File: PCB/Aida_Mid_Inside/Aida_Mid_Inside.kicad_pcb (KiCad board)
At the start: 2 copper layers, 50.3 x 61.6 mm, 24 parts

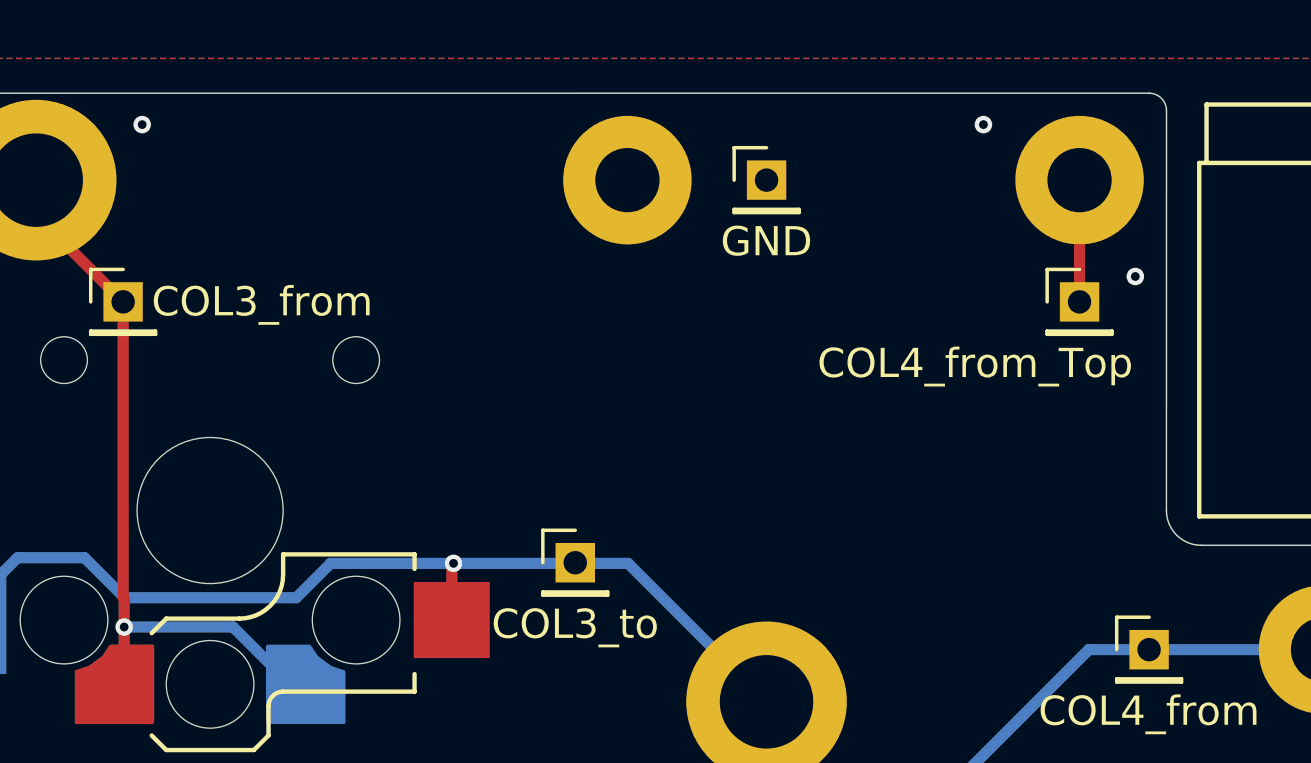
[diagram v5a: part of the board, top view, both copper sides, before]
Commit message: 開発ナンバーと表裏を記載
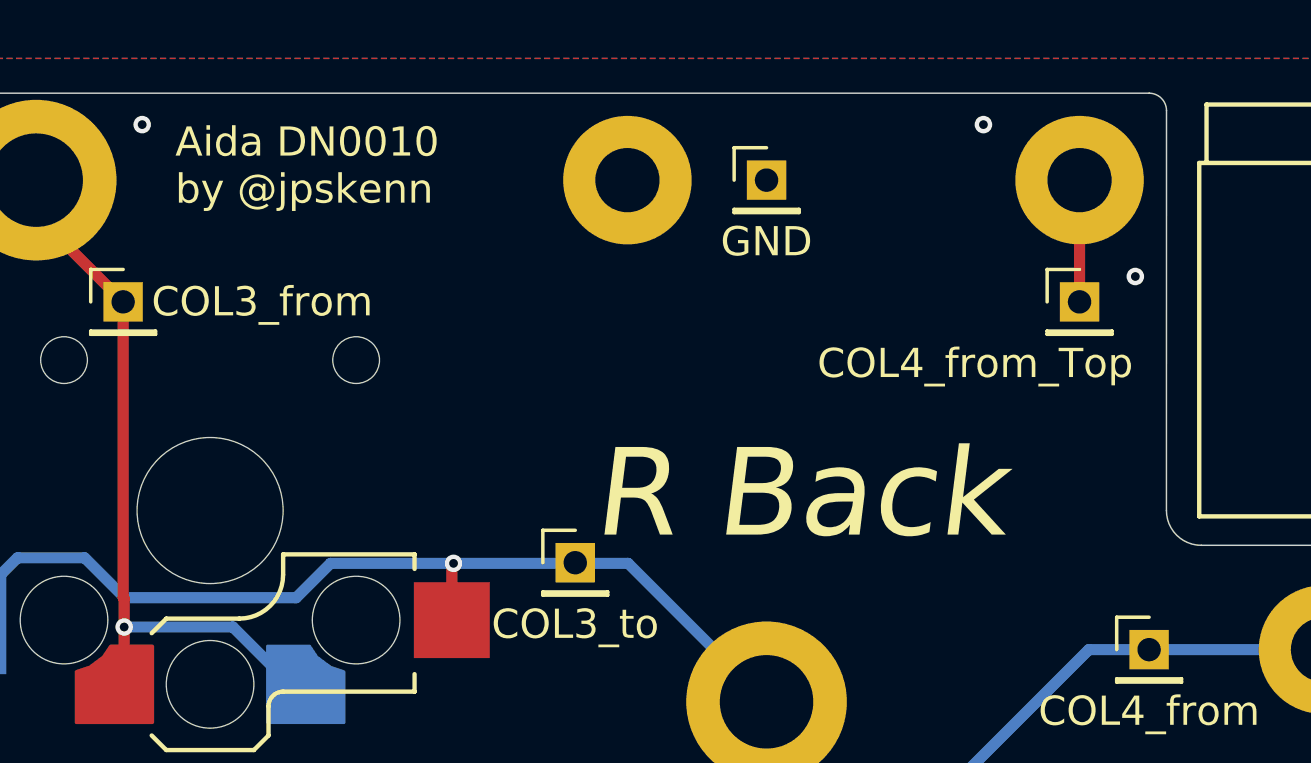
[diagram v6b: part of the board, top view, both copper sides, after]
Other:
- board text added: "Aida DN0010 by @jpskenn"
- board text added: "L Back"
- board text added: "R Back"
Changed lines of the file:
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@@
 		(layer "User.1")
+	)
+	(gr_text "R Back"
+		(at 122.634375 48.815617 0)
+		(layer "F.SilkS" knockout)
+		(effects
+			(font
+				(size 3 3)
+				(thickness 0.375)
+				(italic yes)
+			)
+			(justify left bottom)
+		)
+	)
+	(gr_text "Aida DN0010\nby @jpskenn"
+		(at 108.3451 37.206742 0)
+		(layer "F.SilkS")
+		(effects
+			(font
+				(size 1 1)
+				(thickness 0.1)
+			)
+			(justify left bottom)
+		)
+	)
+	(gr_text "L Back"
+		(at 139.303125 48.815617 0)
+		(layer "B.SilkS" knockout)
+		(effects
+			(font
+				(size 3 3)
+				(thickness 0.375)
+				(italic yes)
+			)
+			(justify left bottom mirror)
+		)
 	)
 	(gr_text "Top PCB outline"

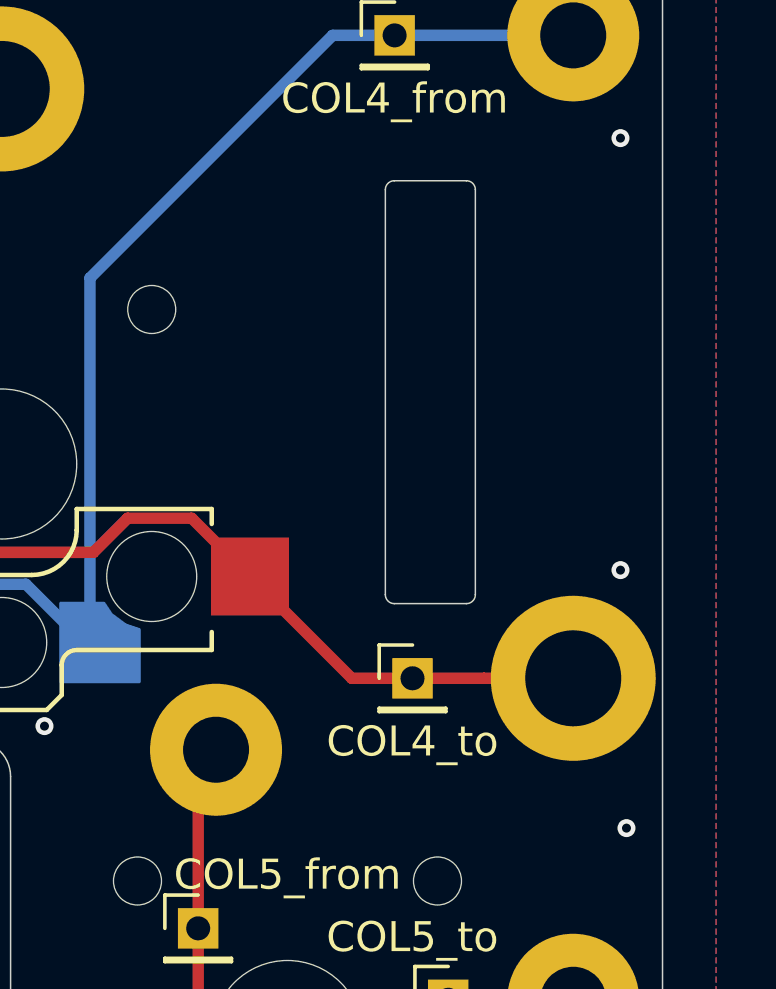
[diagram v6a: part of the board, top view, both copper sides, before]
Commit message: LEDを1/16u下へ移動。 右手のフラッシュメモリとの干渉回避のためボトムプレートの穴位置調整。
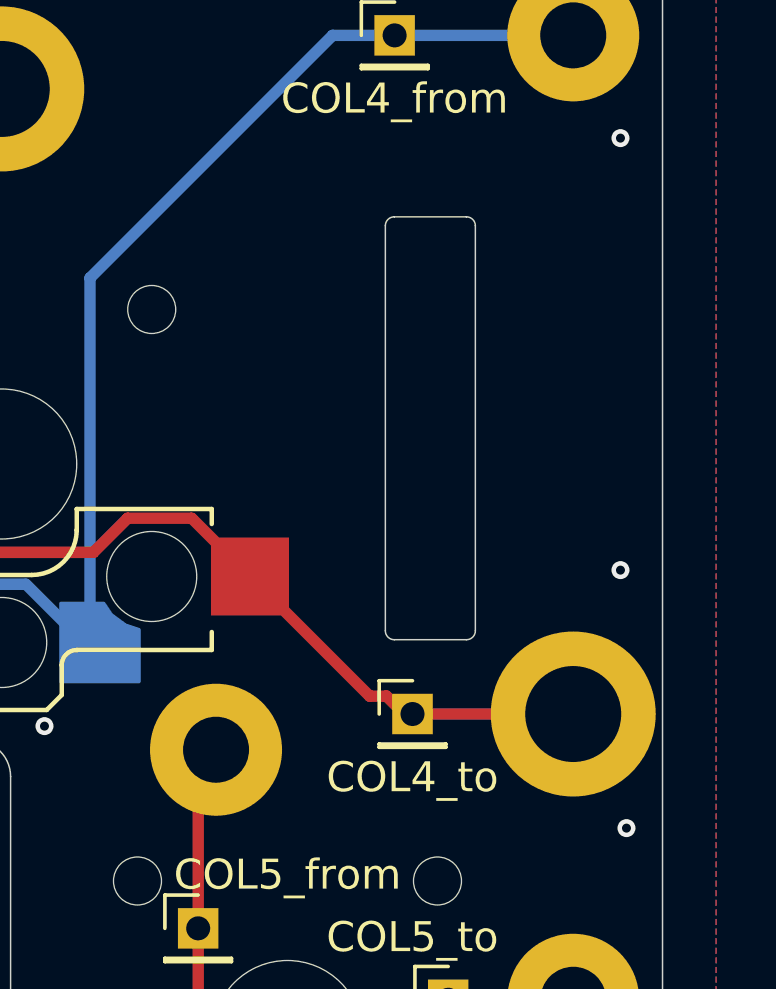
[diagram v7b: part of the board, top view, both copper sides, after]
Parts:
- moved TP5 1.19 mm to (142.3, 75.0)
- moved H5 1.19 mm to (147.6, 75.0)
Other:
- outline, holes or cut-outs redrawn
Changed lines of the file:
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@@
 	(footprint "Connector_PinHeader_2.00mm:PinHeader_1x01_P2.00mm_Vertical"
 		(layer "F.Cu")
-		(at 142.279787 73.818784)
+		(at 142.279787 75.009367)
 		(descr "Through hole straight pin header, 1x01, 2.00mm pitch, single row")
 		(tags "Through hole pin header THT 1x01 2.00mm single row")
@@
 	(footprint "Lib_Local:MountingHole_M2_Through-hole_tap_THC-0.8-1.0-2_minimal"
 		(layer "F.Cu")
-		(at 147.637604 73.818792)
+		(at 147.637604 75.009367)
 		(descr "Mounting Hole 2.2mm, M2")
 		(tags "mounting hole 2.2mm m2")
@@
 	)
 	(gr_line
-		(start 141.67265 57.233592)
-		(end 144.07735 57.233592)
+		(start 141.67265 58.436717)
+		(end 144.07735 58.436717)
 		(stroke
 			(width 0.05)
@@
 	)
 	(gr_arc
-		(start 144.375 71.031242)
-		(mid 144.28782 71.241712)
-		(end 144.07735 71.328892)
+		(start 144.375 72.234367)
+		(mid 144.287809 72.444828)
+		(end 144.07735 72.532017)
 		(stroke
 			(width 0.05)
@@
 	)
 	(gr_arc
-		(start 141.67265 71.328892)
-		(mid 141.46218 71.241712)
-		(end 141.375 71.031242)
+		(start 141.67265 72.532017)
+		(mid 141.462197 72.444822)
+		(end 141.375 72.234367)
 		(stroke
 			(width 0.05)
@@
 	)
 	(gr_line
-		(start 144.07735 71.328892)
-		(end 141.67265 71.328892)
+		(start 144.07735 72.532017)
+		(end 141.67265 72.532017)
 		(stroke
 			(width 0.05)
@@
 	)
 	(gr_line
-		(start 141.375 57.531242)
-		(end 141.375 71.031242)
+		(start 141.375 58.734367)
+		(end 141.375 72.234367)
 		(stroke
 			(width 0.05)
@@
 	)
 	(gr_arc
-		(start 141.375 57.531242)
-		(mid 141.46218 57.320772)
-		(end 141.67265 57.233592)
+		(start 141.375 58.734367)
+		(mid 141.462162 58.523852)
+		(end 141.67265 58.436717)
 		(stroke
 			(width 0.05)
@@
 	)
 	(gr_arc
-		(start 144.07735 57.233592)
-		(mid 144.28782 57.320772)
-		(end 144.375 57.531242)
+		(start 144.07735 58.436717)
+		(mid 144.287773 58.523917)
+		(end 144.375 58.734367)
 		(stroke
 			(width 0.05)
@@
 	)
 	(gr_line
-		(start 144.375 57.531242)
-		(end 144.375 71.031242)
+		(start 144.375 58.734367)
+		(end 144.375 72.234367)
 		(stroke
 			(width 0.05)
@@
 		(layer "Dwgs.User")
 		(pts
-			(xy 141.375 57.531242) (xy 144.375 57.531242)
+			(xy 141.375 58.734367) (xy 144.375 58.734367)
 		)
 		(height -2)
@@
 		)
 		(gr_text "3"
-			(at 142.875 54.381242 0)
+			(at 142.875 55.584367 0)
 			(layer "Dwgs.User")
 			(effects
@@
 		(layer "Dwgs.User")
 		(pts
-			(xy 141.375 57.531242) (xy 141.375 71.031242)
+			(xy 141.375 58.734367) (xy 141.375 72.234367)
 		)
 		(height -1)
@@
 		)
 		(gr_text "13.5"
-			(at 139.225 64.281242 90)
+			(at 139.225 65.484367 90)
 			(layer "Dwgs.User")
 			(effects
@@
 	)
 	(segment
-		(start 140.256284 73.818784)
-		(end 136.8625 70.425)
+		(start 142.009375 75.009367)
+		(end 141.4125 74.412492)
 		(width 0.381)
 		(layer "F.Cu")
@@
 	)
 	(segment
-		(start 144.661031 73.818792)
-		(end 144.661023 73.818784)
+		(start 140.849992 74.412492)
+		(end 136.8625 70.425)
 		(width 0.381)
 		(layer "F.Cu")
@@
 	)
 	(segment
-		(start 144.661023 73.818784)
-		(end 142.279787 73.818784)
+		(start 142.279787 75.009367)
+		(end 142.009375 75.009367)
 		(width 0.381)
 		(layer "F.Cu")
@@
 	)
 	(segment
-		(start 142.279787 73.818784)
-		(end 140.256284 73.818784)
+		(start 132.783304 68.4835)
+		(end 134.921 68.4835)
 		(width 0.381)
 		(layer "F.Cu")
@@
 	)
 	(segment
-		(start 132.783304 68.4835)
-		(end 134.921 68.4835)
+		(start 141.4125 74.412492)
+		(end 140.849992 74.412492)
 		(width 0.381)
 		(layer "F.Cu")
@@
 	)
 	(segment
-		(start 147.637604 73.818792)
-		(end 144.661031 73.818792)
+		(start 131.646 69.620804)
+		(end 132.783304 68.4835)
 		(width 0.381)
 		(layer "F.Cu")
@@
 	)
 	(segment
-		(start 131.646 69.620804)
-		(end 132.783304 68.4835)
+		(start 147.637604 75.009367)
+		(end 142.279787 75.009367)
 		(width 0.381)
 		(layer "F.Cu")
